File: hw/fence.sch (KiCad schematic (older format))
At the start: 9 parts, among them J1 Conn_01x02_Male, J2 Conn_01x08_Female, J3 Conn_01x02_Male, J4 Conn_01x08_Female, J5 Conn_01x04_Male, U1 4N25, U2 4N25

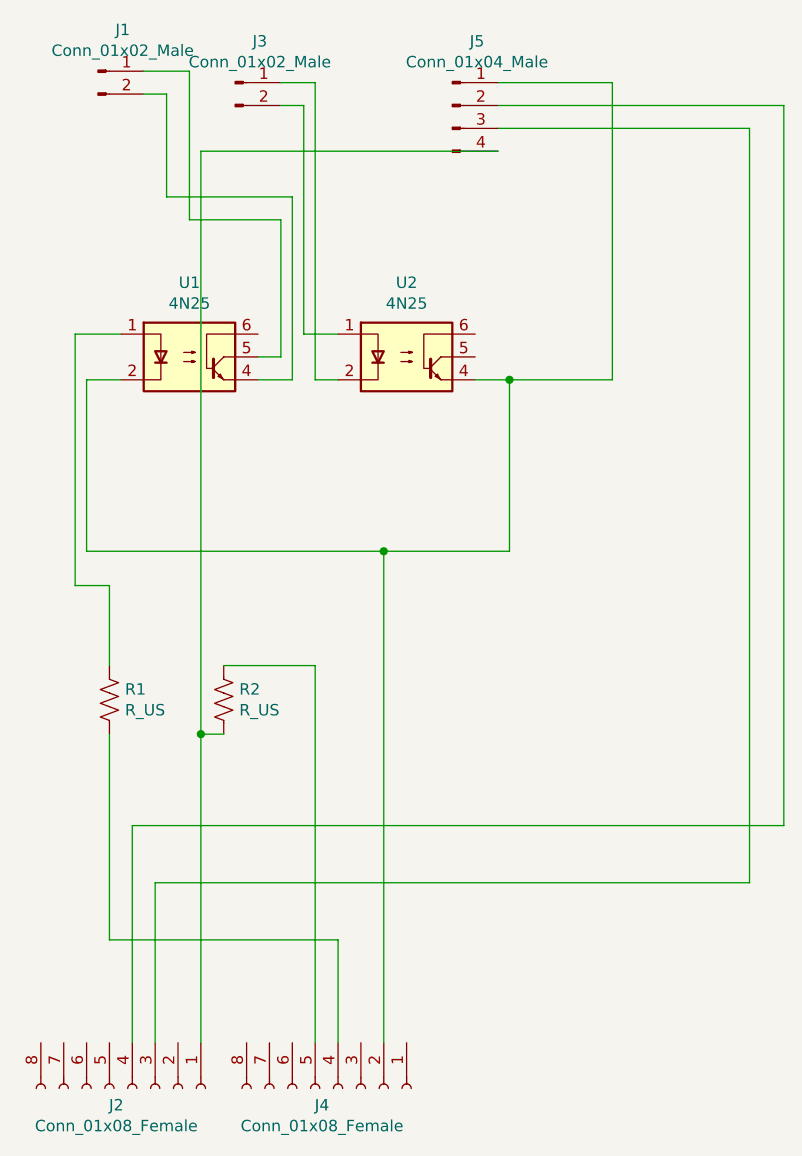
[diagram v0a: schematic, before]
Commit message: Fix: WeMos pin5 leftover
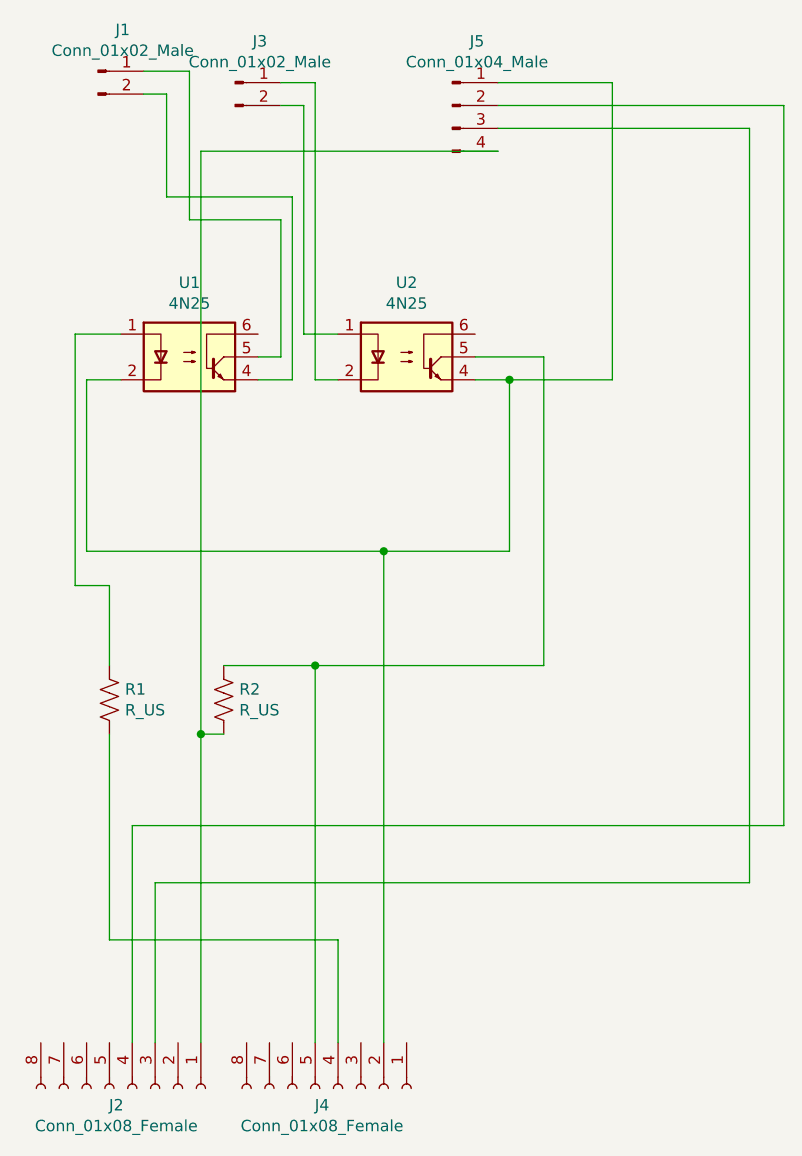
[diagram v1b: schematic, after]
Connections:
- net at J4.5 (Pin_5), R2.1: now also U2.5
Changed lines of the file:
@@
 Wire Wire Line
 	2000 6800 2000 7250
+Wire Wire Line
+	2600 4250 2900 4250
+Wire Wire Line
+	2900 4250 2900 5600
+Wire Wire Line
+	2900 5600 1900 5600
+Connection ~ 1900 5600
 $EndSCHEMATC

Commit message: Bundle update
* pcb refactor & fixes
* schetch minor cosmethics
* html buttons rename and synchronization with indicators
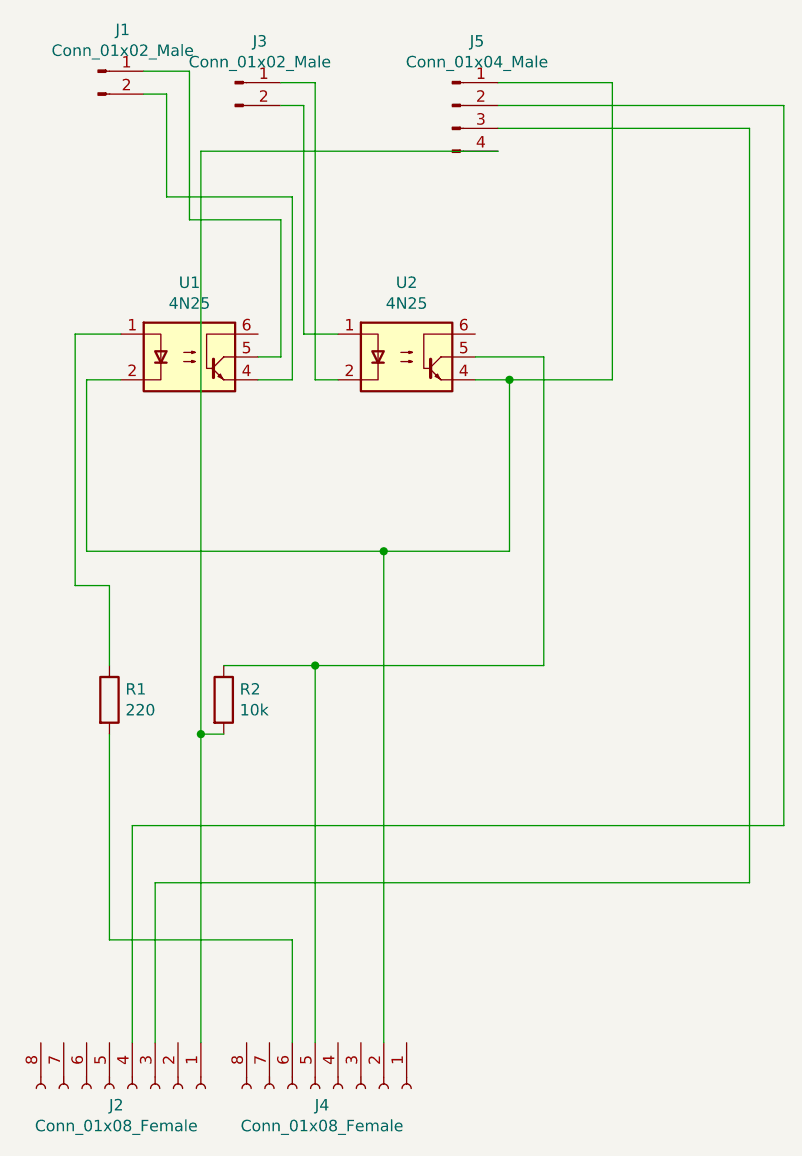
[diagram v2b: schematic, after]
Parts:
- removed R1, R2: R_US, Resistor_THT:R_Axial_DIN0204_L3.6mm_D1.6mm_P5.08mm_Horizontal, symbol Device:R_US
- added R1: 220, Resistor_THT:R_Axial_DIN0207_L6.3mm_D2.5mm_P10.16mm_Horizontal, symbol Device:R
- added R2: 10k, Resistor_THT:R_Axial_DIN0207_L6.3mm_D2.5mm_P10.16mm_Horizontal, symbol Device:R
- J1, J3: footprint Connector_PinSocket_2.54mm:PinSocket_1x02_P2.54mm_Vertical -> Connector_PinHeader_2.54mm:PinHeader_1x02_P2.54mm_Vertical
- J5: footprint Connector_PinSocket_2.54mm:PinSocket_1x04_P2.54mm_Vertical -> Connector_PinHeader_2.54mm:PinHeader_1x04_P2.54mm_Vertical
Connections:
- net at J2.1 (Pin_1), J5.4 (Pin_4): now also R2.2
- net at J4.5 (Pin_5), U2.5: now also R2.1
- net at J4.6 (Pin_6): now also R1.2
- net at U1.1: now also R1.1
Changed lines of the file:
@@
-$EndComp
-$Comp
-L Device:R_US R1
-U 1 1 63AC7796
-P 1000 5750
-F 0 "R1" H 1068 5796 50  0000 L CNN
-F 1 "R_US" H 1068 5705 50  0000 L CNN
-F 2 "Resistor_THT:R_Axial_DIN0204_L3.6mm_D1.6mm_P5.08mm_Horizontal" V 1040 5740 50  0001 C CNN
-F 3 "~" H 1000 5750 50  0001 C CNN
-	1    1000 5750
-	1    0    0    -1
-$EndComp
-$Comp
-L Device:R_US R2
-U 1 1 63AC8D95
-P 1500 5750
-F 0 "R2" H 1568 5796 50  0000 L CNN
-F 1 "R_US" H 1568 5705 50  0000 L CNN
-F 2 "Resistor_THT:R_Axial_DIN0204_L3.6mm_D1.6mm_P5.08mm_Horizontal" V 1540 5740 50  0001 C CNN
-F 3 "~" H 1500 5750 50  0001 C CNN
-	1    1500 5750
-	1    0    0    -1
 $EndComp
 $Comp
@@
 F 0 "J1" H 1058 3181 50  0000 C CNN
 F 1 "Conn_01x02_Male" H 1058 3090 50  0000 C CNN
-F 2 "Connector_PinSocket_2.54mm:PinSocket_1x02_P2.54mm_Vertical" H 950 3000 50  0001 C CNN
+F 2 "Connector_PinHeader_2.54mm:PinHeader_1x02_P2.54mm_Vertical" H 950 3000 50  0001 C CNN
 F 3 "~" H 950 3000 50  0001 C CNN
 	1    950  3000
@@
 F 0 "J3" H 1658 3231 50  0000 C CNN
 F 1 "Conn_01x02_Male" H 1658 3140 50  0000 C CNN
-F 2 "Connector_PinSocket_2.54mm:PinSocket_1x02_P2.54mm_Vertical" H 1550 3050 50  0001 C CNN
+F 2 "Connector_PinHeader_2.54mm:PinHeader_1x02_P2.54mm_Vertical" H 1550 3050 50  0001 C CNN
 F 3 "~" H 1550 3050 50  0001 C CNN
 	1    1550 3050
@@
 F 0 "J5" H 2608 3431 50  0000 C CNN
 F 1 "Conn_01x04_Male" H 2608 3340 50  0000 C CNN
-F 2 "Connector_PinSocket_2.54mm:PinSocket_1x04_P2.54mm_Vertical" H 2500 3150 50  0001 C CNN
+F 2 "Connector_PinHeader_2.54mm:PinHeader_1x04_P2.54mm_Vertical" H 2500 3150 50  0001 C CNN
 F 3 "~" H 2500 3150 50  0001 C CNN
 	1    2500 3150
@@
 Wire Wire Line
 	1400 5900 1400 3350
-Wire Wire Line
-	1900 7250 1900 5600
-Wire Wire Line
-	1900 5600 1500 5600
 Wire Wire Line
 	2200 5100 2750 5100
@@
 	1000 5900 1000 6800
 Wire Wire Line
-	1000 6800 2000 6800
-Wire Wire Line
-	2000 6800 2000 7250
-Wire Wire Line
 	2600 4250 2900 4250
 Wire Wire Line
 	2900 4250 2900 5600
+$Comp
+L Device:R R1
+U 1 1 63B82D6D
+P 1000 5750
+F 0 "R1" H 1070 5796 50  0000 L CNN
+F 1 "220" H 1070 5705 50  0000 L CNN
+F 2 "Resistor_THT:R_Axial_DIN0207_L6.3mm_D2.5mm_P10.16mm_Horizontal" V 930 5750 50  0001 C CNN
+F 3 "~" H 1000 5750 50  0001 C CNN
+	1    1000 5750
+	1    0    0    -1
+$EndComp
+$Comp
+L Device:R R2
+U 1 1 63B8378D
+P 1500 5750
+F 0 "R2" H 1570 5796 50  0000 L CNN
+F 1 "10k" H 1570 5705 50  0000 L CNN
+F 2 "Resistor_THT:R_Axial_DIN0207_L6.3mm_D2.5mm_P10.16mm_Horizontal" V 1430 5750 50  0001 C CNN
+F 3 "~" H 1500 5750 50  0001 C CNN
+	1    1500 5750
+	1    0    0    -1
+$EndComp
 Wire Wire Line
-	2900 5600 1900 5600
+	1800 7250 1800 6800
+Wire Wire Line
+	1000 6800 1800 6800
+Wire Wire Line
+	1900 7250 1900 5600
+Wire Wire Line
+	1500 5600 1900 5600
+Wire Wire Line
+	1900 5600 2900 5600
 Connection ~ 1900 5600
 $EndSCHEMATC
